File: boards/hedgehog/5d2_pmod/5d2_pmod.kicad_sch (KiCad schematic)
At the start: 23 parts

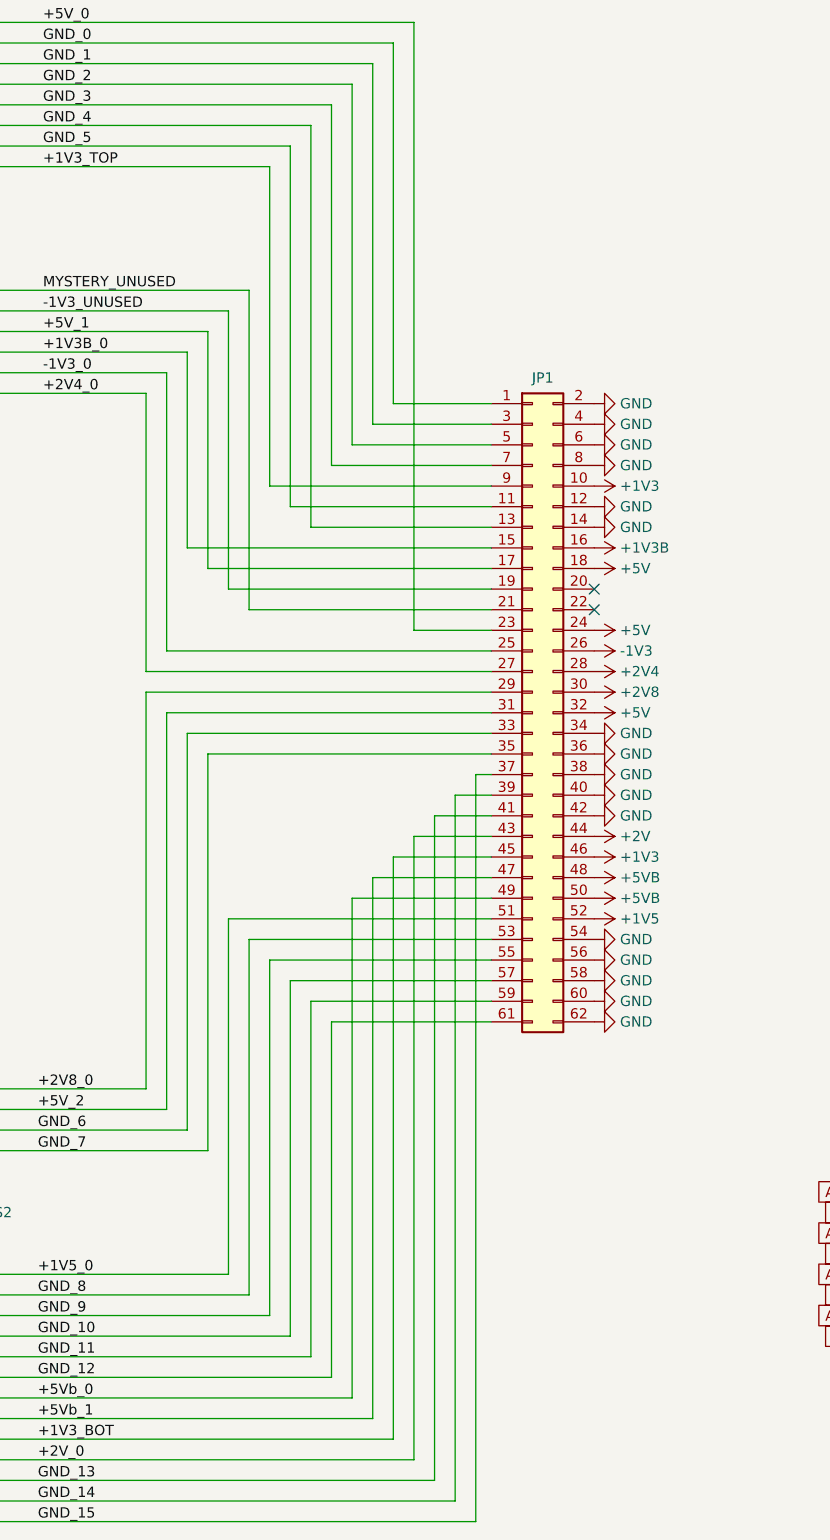
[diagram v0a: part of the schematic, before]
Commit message: secend revision of hedgehog/5d2_pmod board
the first revision sadly had wrong row spacing for the sensor connectors and was thus unusable
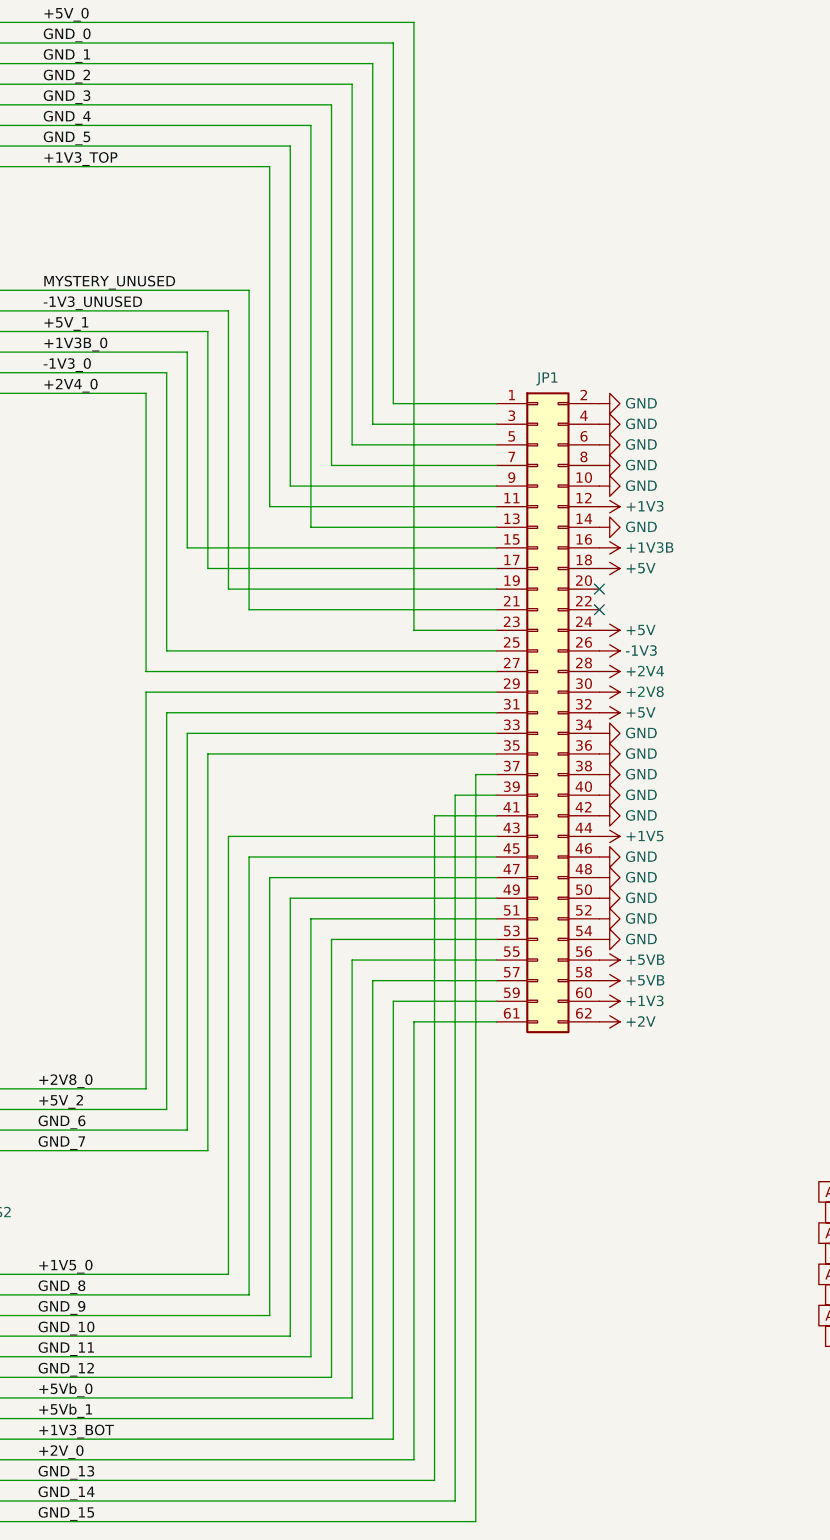
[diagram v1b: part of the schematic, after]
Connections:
- net +1V3: now also JP1.12 (Pin_12), JP1.60 (Pin_60); no longer JP1.10 (Pin_10), JP1.46 (Pin_46)
- net +1V3_BOT: now also JP1.59 (Pin_59); no longer JP1.45 (Pin_45)
- net +1V3_TOP: now also JP1.11 (Pin_11); no longer JP1.9 (Pin_9)
- net +1V5: now also JP1.44 (Pin_44); no longer JP1.52 (Pin_52)
- net +1V5_0: now also JP1.43 (Pin_43); no longer JP1.51 (Pin_51)
- net +2V: now also JP1.62 (Pin_62); no longer JP1.44 (Pin_44)
- net +2V_0: now also JP1.61 (Pin_61); no longer JP1.43 (Pin_43)
- net +5VB: now also JP1.56 (Pin_56), JP1.58 (Pin_58); no longer JP1.48 (Pin_48), JP1.50 (Pin_50)
- net +5Vb_0: now also JP1.55 (Pin_55); no longer JP1.49 (Pin_49)
- net +5Vb_1: now also JP1.57 (Pin_57); no longer JP1.47 (Pin_47)
- net GND: now also JP1.10 (Pin_10), JP1.46 (Pin_46), JP1.48 (Pin_48), JP1.50 (Pin_50), JP1.52 (Pin_52); no longer JP1.12 (Pin_12), JP1.56 (Pin_56), JP1.58 (Pin_58), JP1.60 (Pin_60), JP1.62 (Pin_62)
- net GND_10: now also JP1.49 (Pin_49); no longer JP1.57 (Pin_57)
- net GND_11: now also JP1.51 (Pin_51); no longer JP1.59 (Pin_59)
- net GND_12: now also JP1.53 (Pin_53); no longer JP1.61 (Pin_61)
- net GND_5: now also JP1.9 (Pin_9); no longer JP1.11 (Pin_11)
- net GND_8: now also JP1.45 (Pin_45); no longer JP1.53 (Pin_53)
- net GND_9: now also JP1.47 (Pin_47); no longer JP1.55 (Pin_55)
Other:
- moved on the sheet: JP1
